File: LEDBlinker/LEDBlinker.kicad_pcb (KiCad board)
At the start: 2 copper layers, 83 x 38 mm, 26 parts, among them J1 USB-C Breakout, SW1 SW_SPDT, U1 LM555xN, U2 CD4017BE

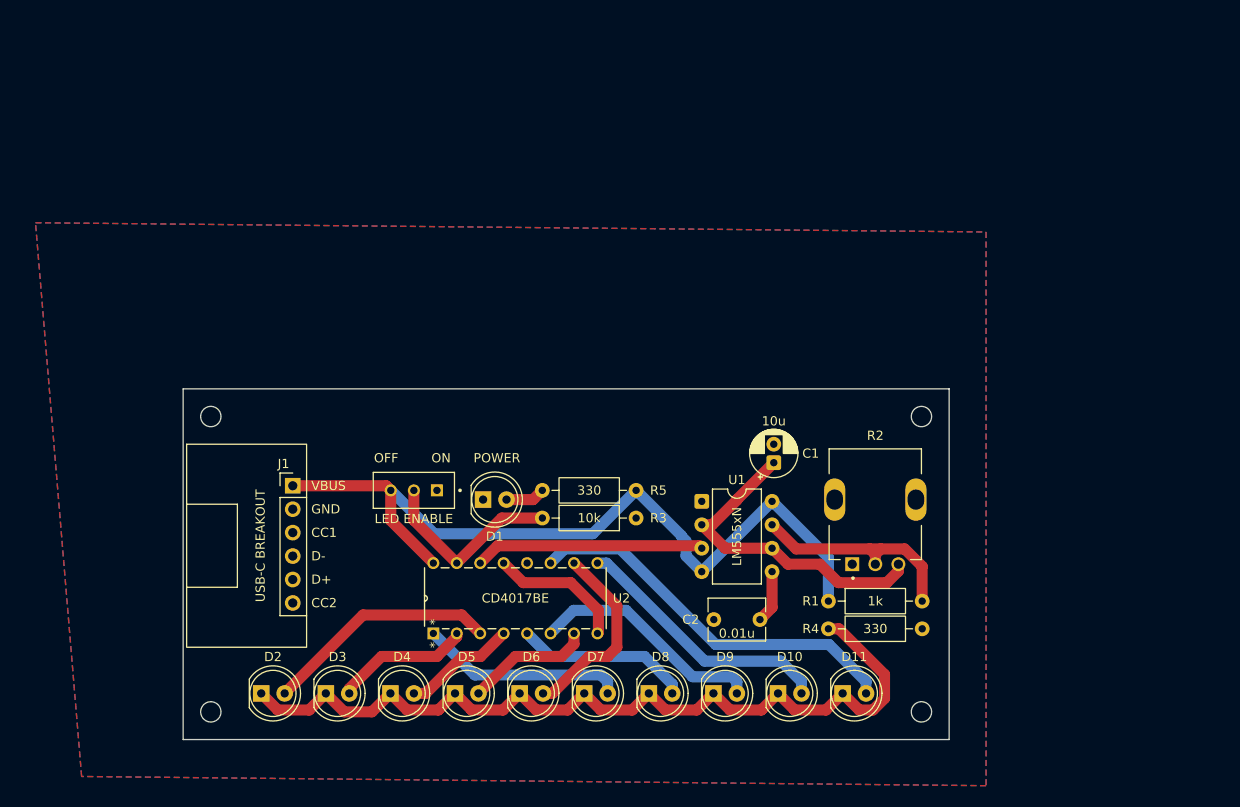
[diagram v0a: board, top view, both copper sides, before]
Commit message: Added more space for components
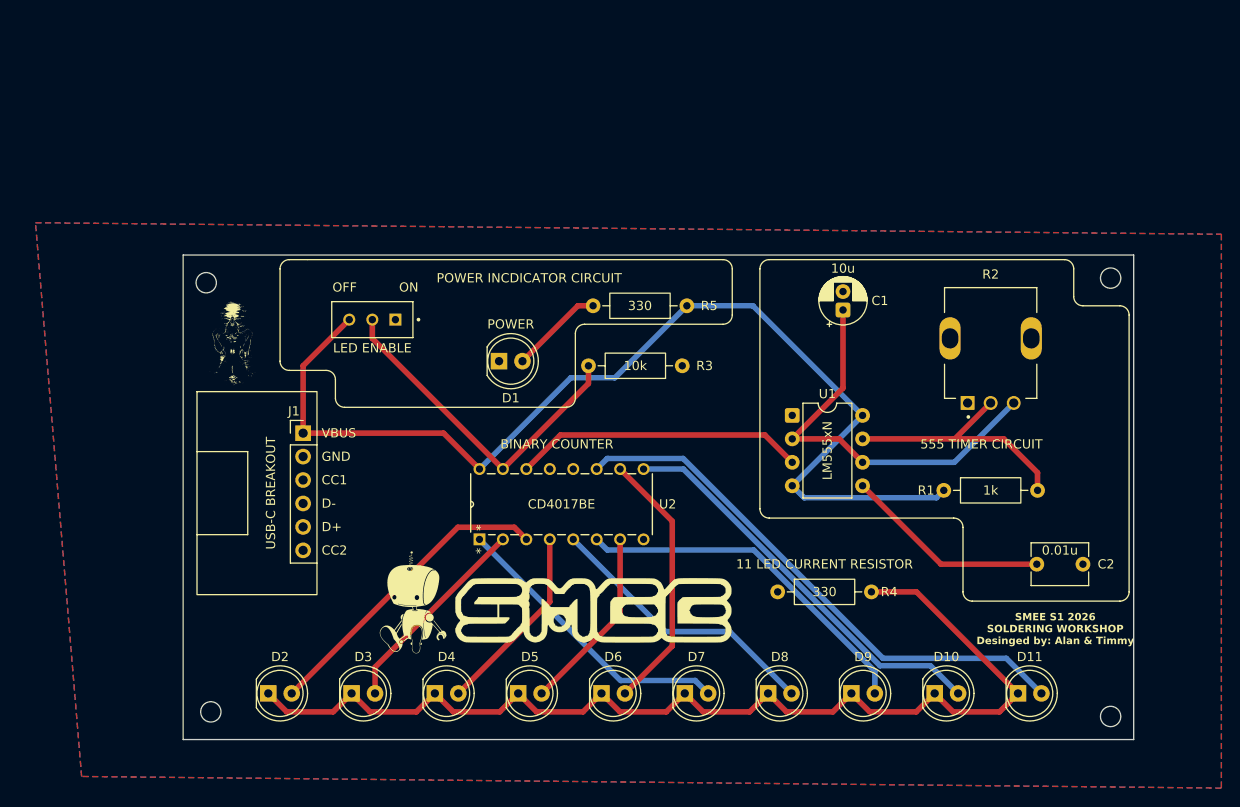
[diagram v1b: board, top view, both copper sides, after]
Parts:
- added G***: LOGO, LOGO, F.Cu at (105.0, 75.0)
- added G***: LOGO, LOGO, F.Cu at (144.0, 104.0)
- added G***: LOGO, LOGO, F.Cu at (124.0, 103.0)
- moved C2 30.6 mm to (192.0, 99.0), turned to 0 degrees
- moved H2 25.4 mm to (200.0, 68.0)
- moved R2 21.5 mm to (187.0, 74.5)
- moved R5 20.7 mm to (154.1, 71.0)
- moved H4 20.5 mm to (200.0, 115.5)
- moved SW1 19.0 mm to (120.0, 72.5)
- moved D11 19.0 mm to (190.0, 113.0)
- moved C1 18.2 mm to (171.0, 71.5)
- moved R1 17.3 mm to (181.9, 91.0)
- moved R3 17.2 mm to (153.6, 77.5)
- moved D10 17.0 mm to (180.9, 113.0)
- moved R4 16.2 mm to (163.9, 102.0), turned to 0 degrees
- moved D1 15.1 mm to (133.7, 77.0)
- moved D9 14.9 mm to (171.9, 113.0)
- moved H1 14.5 mm to (102.0, 68.5)
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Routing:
- net +5V: track 87.0 -> 116.9 mm
- net Net-(D10-K): track 93.2 -> 116.6 mm
- net Net-(D11-A): track 42.1 -> 59.2 mm
- net Net-(U1-CONT): track 5.73 -> 22.4 mm
- net Net-(SW1-B): track 21.1 -> 37.1 mm
- net Net-(D10-A): track 28.7 -> 44.2 mm
- net GND: track 14.9 -> 0.00 mm
- net Net-(D9-A): track 25.7 -> 38.5 mm
- net Net-(D8-A): track 19.0 -> 30.6 mm
- net Net-(D7-A): track 22.3 -> 31.7 mm
- net Net-(D4-A): track 12.4 -> 20.8 mm
- net Net-(U1-THRES): track 35.8 -> 44.0 mm
- net Net-(D2-A): track 25.5 -> 33.4 mm
- net Net-(D6-A): track 21.1 -> 28.8 mm
- net Net-(D3-A): track 14.8 -> 22.4 mm
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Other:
- board size 83 x 38 mm -> 103 x 52.5 mm
- board text added: "11 LED CURRENT RESISTOR"
- board text added: "555 TIMER CIRCUIT"
- board text added: "BINARY COUNTER"
- board text added: "POWER INCDICATOR CIRCUIT"
- board text added: "SMEE S1 2026 SOLDERING WORKSHOP Desinged by: Alan & Timmy"

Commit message: Add images/backups; update PCB footprint/logo
Modify LEDBlinker.kicad_pcb: remove a zone_defaults line and replace/update a footprint (previous LED_THT entry replaced with a LOGO footprint), adjust properties (Reference/Value/Description/hide flags), and regenerate many silkscreen/fp_poly/fp_* elements (coordinates, styles and UUIDs updated). Also add/rename local lock files (~LEDBlinker.kicad_pcb.lck and ~LEDBlinker.kicad_sch.lck). These changes appear to apply a redesigned silkscreen/logo and related footprint metadata updates.
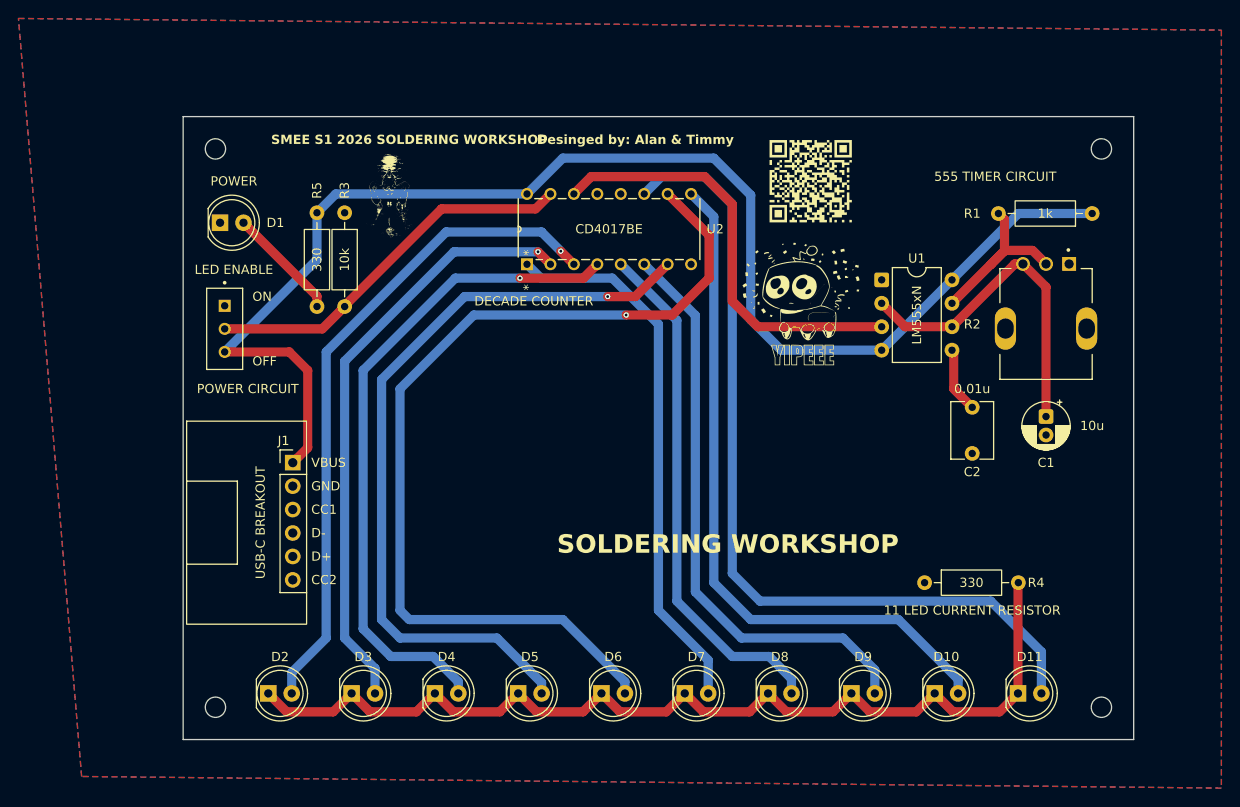
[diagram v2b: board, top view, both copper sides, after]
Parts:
- removed the G*** at (144.0, 104.0)
- removed the G*** at (124.0, 103.0)
- added G***: LOGO, LOGO, F.Cu at (166.5, 71.0)
- added G***: LOGO, LOGO, F.Cu at (131.0, 88.8)
- added G***: LOGO, LOGO, F.Cu at (158.0, 89.0)
- added G***: LOGO, LOGO, F.Cu at (167.5, 57.5)
- added G***: LOGO, LOGO, B.Cu at (150.0, 90.0)
- moved R5 41.3 mm to (114.0, 60.9), turned to -90 degrees
- moved R3 40.2 mm to (117.0, 60.9), turned to -90 degrees
- moved R1 34.0 mm to (198.0, 61.0), turned to 180 degrees
- moved D1 33.7 mm to (103.5, 62.0)
- moved U2 30.3 mm to (154.5, 58.9)
- moved C1 24.8 mm to (193.0, 83.0), turned to -90 degrees
- moved G*** 23.3 mm to (122.0, 59.0)
- moved C2 18.4 mm to (185.0, 82.0), turned to -90 degrees
- moved U1 17.6 mm to (175.2, 68.2)
- moved SW1 16.0 mm to (104.0, 73.5), turned to -90 degrees
- moved R4 16.0 mm to (179.8, 101.0)
- moved H1 14.5 mm to (103.0, 54.0)
- moved H2 14.0 mm to (199.0, 54.0)
- moved R2 6.09 mm to (193.0, 73.5), turned to 180 degrees
- moved J1 3.39 mm to (111.4, 88.0)
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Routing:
- net Net-(D6-A): track 28.8 -> 102.3 mm, vias 0 -> 1
- net Net-(D5-A): track 20.2 -> 83.5 mm, vias 0 -> 1
- net Net-(D4-A): track 20.8 -> 72.1 mm, vias 0 -> 1
- net Net-(D3-A): track 22.4 -> 65.1 mm, vias 0 -> 1
- net Net-(D2-A): track 33.4 -> 72.2 mm, vias 0 -> 1
- net Net-(D11-A): track 59.2 -> 93.1 mm
- net +5V: track 116.9 -> 148.8 mm
- net Net-(D10-A): track 44.2 -> 75.5 mm
- net Net-(D7-A): track 31.7 -> 59.2 mm
- net Net-(D8-A): track 30.6 -> 56.5 mm
- net Net-(D9-A): track 38.5 -> 63.3 mm
- net /OUT: track 31.6 -> 47.0 mm
- net Net-(U1-CONT): track 22.4 -> 7.10 mm
- net Net-(D10-K): track 116.6 -> 108.2 mm
- net Net-(U1-DISCH): track 28.0 -> 19.6 mm
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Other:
- board size 103 x 52.5 mm -> 103 x 67.5 mm
- board text added: "DECADE COUNTER"
- board text added: "Desinged by: Alan & Timmy"
- board text added: "POWER CIRCUIT"
- board text added: "SMEE S1 2026 SOLDERING WORKSHOP"
- board text added: "SOLDERING WORKSHOP"
- board text removed: "BINARY COUNTER"
- board text removed: "POWER INCDICATOR CIRCUIT"
- board text removed: "SMEE S1 2026 SOLDERING WORKSHOP Desinged by: Alan & Timmy"

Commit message: Spaced out more
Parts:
- removed the G*** at (122.0, 59.0)
- removed the G*** at (167.5, 57.5)
- moved R3 6.00 mm to (123.0, 60.9)
- moved C2 5.32 mm to (181.0, 85.5)
- moved C1 4.04 mm to (193.0, 87.0)
- moved R1 2.00 mm to (198.0, 59.0)
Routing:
- net Net-(U1-THRES): track 36.7 -> 40.8 mm
- net Net-(SW1-B): track 41.4 -> 44.9 mm
- net Net-(U1-CONT): track 7.10 -> 10.6 mm
- net Net-(U1-DISCH): track 19.6 -> 21.1 mm
- net +5V: track 148.8 -> 149.7 mm

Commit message: Final commit before purchase
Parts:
- added G***: LOGO, LOGO, F.Cu at (167.5, 58.5)
- C1: footprint Capacitor_THT:CP_Radial_D5.0mm_P2.00mm -> Capacitor_THT:CP_Radial_D5.0mm_P2.50mm
- moved R3 4.30 mm to (120.5, 57.4)
- moved R5 3.50 mm to (114.0, 57.4)
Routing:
- net +5V: track 149.7 -> 155.3 mm
- net Net-(SW1-B): track 44.9 -> 41.4 mm
- net Net-(D1-A): track 12.4 -> 10.3 mm
